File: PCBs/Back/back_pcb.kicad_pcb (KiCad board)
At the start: 2 copper layers, 67 x 88.9 mm, 15 parts, among them J1 front joystick, J17 d-pad pins, J18 misc pins, J2 bottom joystick, J3 Conn_01x17_Pin, J4 Arduino, SW1 Left Trigger, SW13 A, SW14 X, SW15 Y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

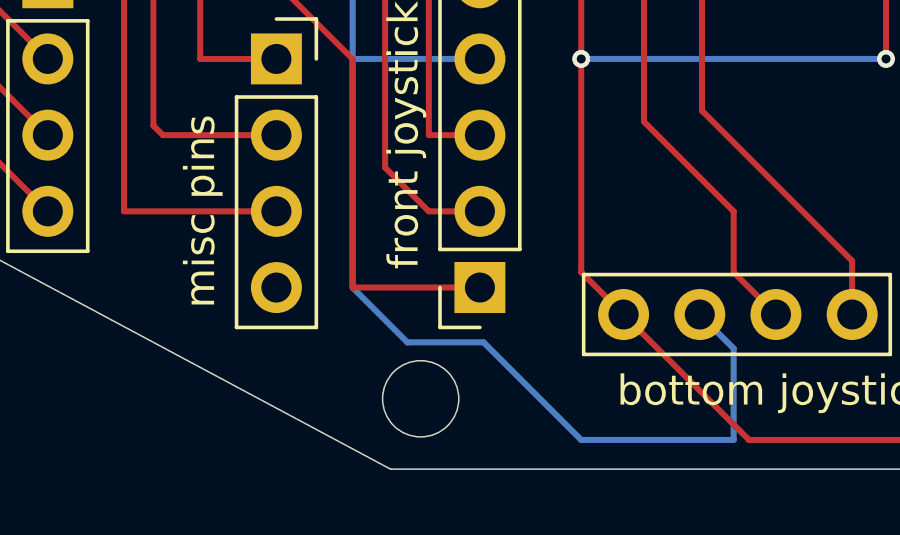
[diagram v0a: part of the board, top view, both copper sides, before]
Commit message: 🐛 add missing gnd connection
- missing gnd connection to the misc pins
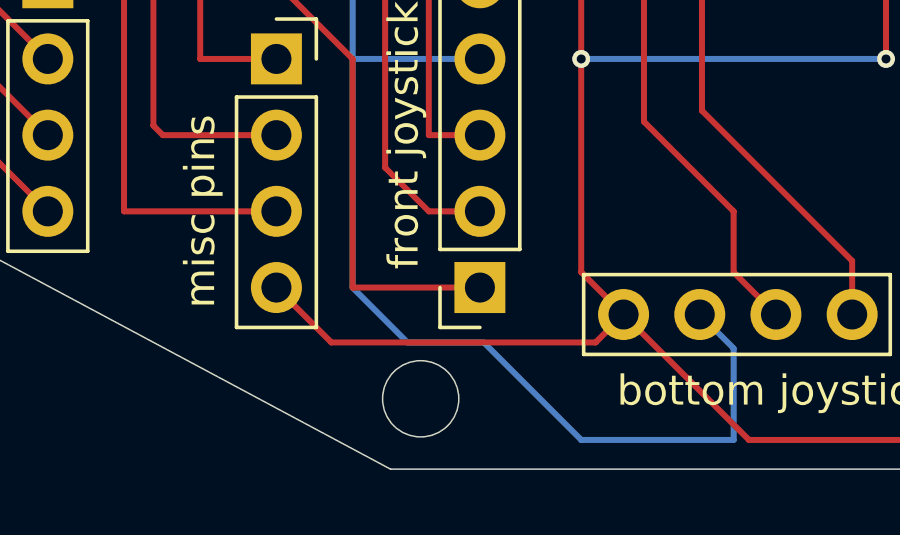
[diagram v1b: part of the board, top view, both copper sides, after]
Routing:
- net /GND: track 205.0 -> 217.7 mm
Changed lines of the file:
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@@
+	)
+	(segment
+		(start 89.38014 131.370201)
+		(end 90.311417 130.438924)
+		(width 0.2)
+		(layer "F.Cu")
+		(net 4)
 	)
 	(segment
@@
 	)
 	(segment
+		(start 80.570201 131.370201)
+		(end 89.38014 131.370201)
+		(width 0.2)
+		(layer "F.Cu")
+		(net 4)
+	)
+	(segment
 		(start 94.492493 134.62)
 		(end 109.22 134.62)
@@
 		(width 0.2)
 		(layer "F.Cu")
+		(net 4)
+	)
+	(segment
+		(start 78.74 129.54)
+		(end 80.570201 131.370201)
+		(width 0.2)
+		(layer "F.Cu")
